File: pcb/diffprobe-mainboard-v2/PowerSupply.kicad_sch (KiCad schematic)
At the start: 14 parts, among them J54 AC_P, J55 AC_N, J56 AC_E

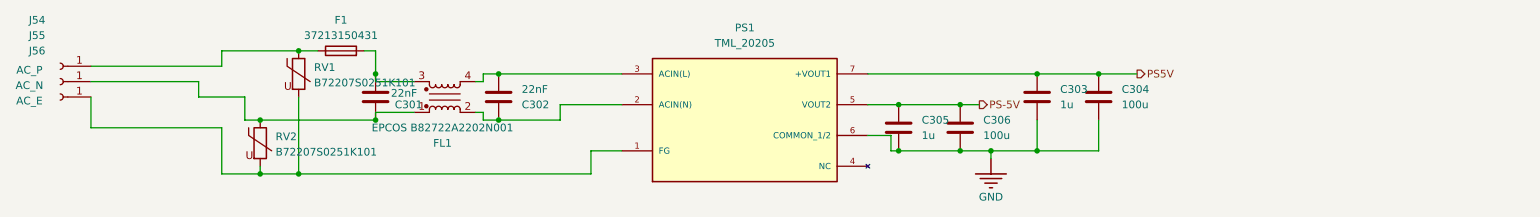
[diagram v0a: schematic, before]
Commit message: KiCAD 9 update, new psu filtering and adc input signal filtering. More silkscreen writing.
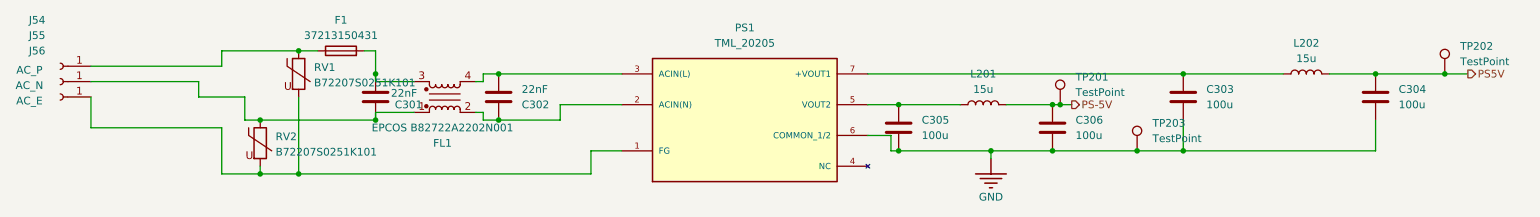
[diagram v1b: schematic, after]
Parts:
- added L201, L202: 15u, Inductor_SMD:L_Ferrocore_DLG-1004, symbol Device:L
- added TP201, TP202, TP203: TestPoint, TestPoint:TestPoint_Pad_D2.0mm, symbol Connector:TestPoint
- C303, C305: value 1u -> 100u; footprint Capacitor_SMD:C_0603_1608Metric -> Capacitor_SMD:C_1206_3216Metric
- C304, C306: footprint Capacitor_SMD:CP_Elec_10x12.5 -> Capacitor_SMD:C_1206_3216Metric
- PS1: footprint Library:CONV_TML_20205 -> MyLib:CONV_TML_20205
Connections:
- net GND: now also TP203.1
- net PS-5V: now also L201.2, TP201.1; no longer C305.1, PS1.5 (VOUT2)
- net PS5V: now also L202.2, TP202.1; no longer C303.1, PS1.7 (+VOUT1)
- new net: C303.1, L202.1, PS1.7 (+VOUT1)
- new net: C305.1, L201.1, PS1.5 (VOUT2)
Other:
- moved on the sheet: C303, C304, C306
